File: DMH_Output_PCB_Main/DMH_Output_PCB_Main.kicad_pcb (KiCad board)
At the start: 2 copper layers, 49 x 175 mm, 92 parts, among them J0 Conn_01x01, J1 TRS_Jack_6.35mm_Sw, J100 IDC_02x05, J2 TRS_Jack_6.35mm_Sw, J200 IDC_02x05, J23 Conn_01x06, J24 Conn_01x02, J25 Conn_01x02, J26 Conn_01x06_PinHeader, J27 Conn_01x06_PinHeader, J28 Conn_01x06, J29 Conn_01x04_PinHeader, J3 TRS_Jack_6.35mm_Sw, J31 Conn_01x06_PinHeader, J35 Conn_01x02_PinHeader, J36 Conn_01x02_PinHeader, J4 TRS_Jack_6.35mm_Sw, J5 TRS_Jack_6.35mm_Sw, J6 TRS_Jack_6.35mm_Sw, J7 TRS_Jack_6.35mm_Sw, J8 TRS_Jack_6.35mm_Sw, J9 TRS_Jack_6.35mm_Sw, U1 TL072, U11 TL074, U13 NE5532, U15 NE5532, U20 TL072, U8 TL074

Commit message: Adjusted output meter resistors
... and deleted unnecessary notes
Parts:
- R84: value 22K -> 22k
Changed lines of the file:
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@@
 			)
 		)
-		(property "Value" "22K"
+		(property "Value" "22k"
 			(at 3.81 0 0)
 			(layer "B.SilkS")

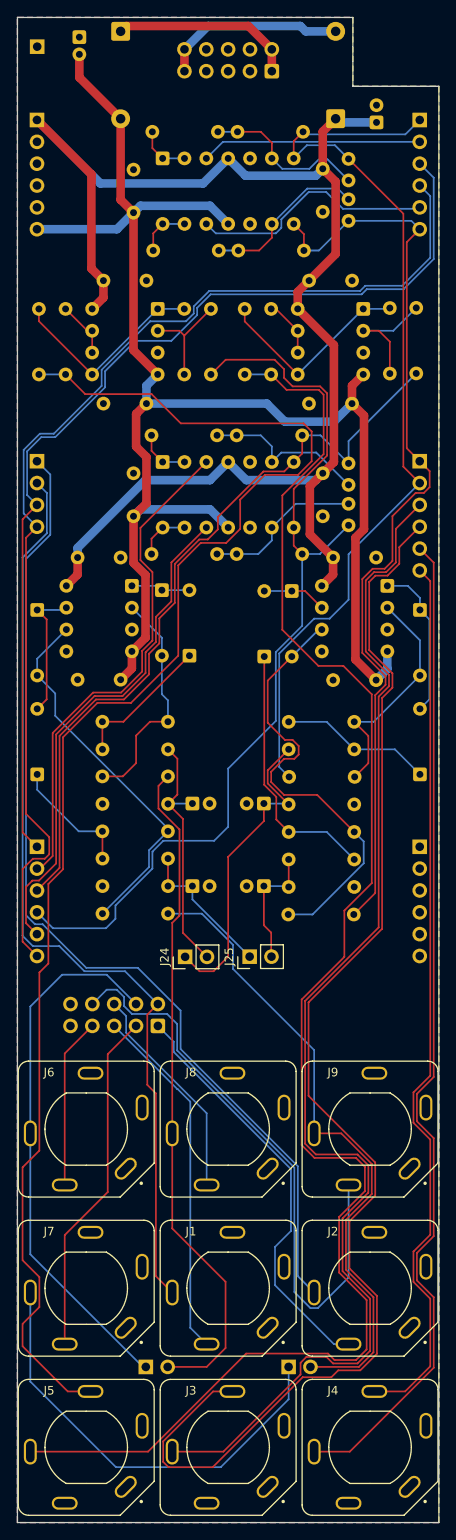
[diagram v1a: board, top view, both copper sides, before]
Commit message: Inverted line outputs hot and cold pins
... in order to avoid phase inversion at the TRS jack tip.
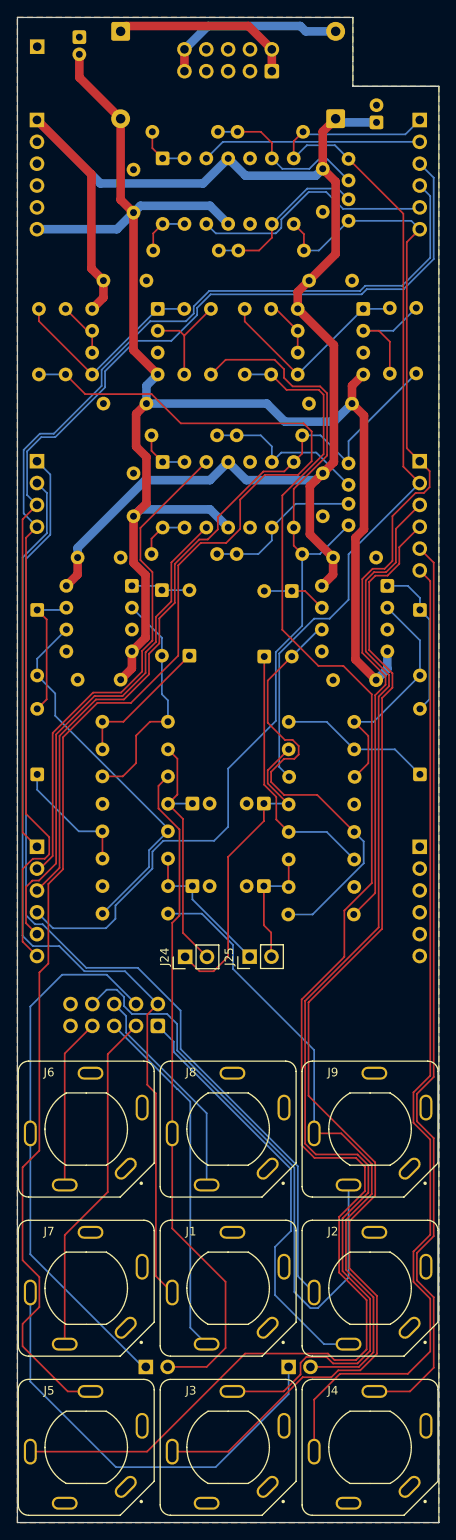
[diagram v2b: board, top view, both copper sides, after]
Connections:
- J31 pad 3: /Balanced Line Driver/L_Bal_OUT_P_M -> /Balanced Line Driver/L_Bal_OUT_N_M
- J31 pad 4: /Balanced Line Driver/L_Bal_OUT_N_M -> /Balanced Line Driver/L_Bal_OUT_P_M
- J31 pad 5: /Balanced Line Driver/R_Bal_OUT_P_M -> /Balanced Line Driver/R_Bal_OUT_N_M
- J31 pad 6: /Balanced Line Driver/R_Bal_OUT_N_M -> /Balanced Line Driver/R_Bal_OUT_P_M
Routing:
- net /Balanced Line Driver/L_Bal_OUT_N_M: track 153.8 -> 134.7 mm
- net /Balanced Line Driver/L_Bal_OUT_P_M: track 144.6 -> 138.9 mm
- net /Balanced Line Driver/R_Bal_OUT_N_M: track 104.0 -> 107.2 mm
- net /Balanced Line Driver/R_Bal_OUT_P_M: track 117.1 -> 116.4 mm
- net Net-(J2-2): track 48.7 -> 49.4 mm
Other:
- board text added: "Mk1.1 July 2026"
- board text removed: "Mk1.0 May 2026"

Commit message: Added test points for easier calibration
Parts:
- added TP21: TestPoint, Connector_Pin:Pin_D1.0mm_L10.0mm, B.Cu at (68.5, 215.3)
- added TP22: TestPoint, Connector_Pin:Pin_D1.0mm_L10.0mm, B.Cu at (76.4, 215.3)
- added TP23: TestPoint, Connector_Pin:Pin_D1.0mm_L10.0mm, B.Cu at (85.0, 215.3)
- added TP24: TestPoint, Connector_Pin:Pin_D1.0mm_L10.0mm, B.Cu at (92.8, 215.3)
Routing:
- net /Balanced Line Driver/L_Bal_OUT_N_M: track 134.7 -> 148.2 mm
- net /Balanced Line Driver/R_Bal_OUT_N_M: track 107.2 -> 120.6 mm
- net /PreAmp/R_Ext_IN_M: track 51.2 -> 41.6 mm
- net /Balanced Line Driver/R_Bal_OUT_P_M: track 116.4 -> 122.5 mm
- net /Balanced Line Driver/L_Bal_OUT_P_M: track 138.9 -> 144.9 mm
